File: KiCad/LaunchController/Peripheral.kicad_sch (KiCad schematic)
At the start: 10 parts, among them J15 CONN_AUDIO, J16 CONN_SPEAKER, J21 RJ45, J22 L, J23 R, U2 24LC256, U7 LTC485CN8#PBF

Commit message: 端子台を選定
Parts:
- J15, J16: footprint Connector_JST:JST_XH_B2B-XH-A_1x02_P2.50mm_Vertical -> TSRP_TerminalBlock_Alphaplus:TB401-1-2-E
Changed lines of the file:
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@@
       (effects (font (size 1.27 1.27)))
     )
-    (property "Footprint" "Connector_JST:JST_XH_B2B-XH-A_1x02_P2.50mm_Vertical" (at 67.31 27.94 0)
-      (effects (font (size 1.27 1.27)) hide)
-    )
-    (property "Datasheet" "https://akizukidenshi.com/catalog/g/gC-12247/" (at 67.31 27.94 0)
+    (property "Footprint" "TSRP_TerminalBlock_Alphaplus:TB401-1-2-E" (at 67.31 27.94 0)
+      (effects (font (size 1.27 1.27)) hide)
+    )
+    (property "Datasheet" "https://akizukidenshi.com/catalog/g/gP-01404/" (at 67.31 27.94 0)
       (effects (font (size 1.27 1.27)) hide)
     )
@@
       (effects (font (size 1.27 1.27)))
     )
-    (property "Footprint" "Connector_JST:JST_XH_B2B-XH-A_1x02_P2.50mm_Vertical" (at 67.31 46.99 0)
-      (effects (font (size 1.27 1.27)) hide)
-    )
-    (property "Datasheet" "https://akizukidenshi.com/catalog/g/gC-12247/" (at 67.31 46.99 0)
-      (effects (font (size 1.27 1.27)) hide)
-    )
+    (property "Footprint" "TSRP_TerminalBlock_Alphaplus:TB401-1-2-E" (at 67.31 46.99 0)
+      (effects (font (size 1.27 1.27)) hide)
+    )
+    (property "Datasheet" "https://akizukidenshi.com/catalog/g/gP-01404/" (at 67.31 46.99 0)
+      (effects (font (size 1.27 1.27)) hide)
+    )

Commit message: 配線終わらん
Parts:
- removed J21: RJ45, Connector_RJ:RJ45_Wuerth_7499010001A_Horizontal, symbol Connector:RJ45
- removed J22: L, Connector_PinHeader_2.54mm:PinHeader_1x08_P2.54mm_Vertical, symbol Connector:Conn_01x08_Socket
- removed J23: R, Connector_PinHeader_2.54mm:PinHeader_1x08_P2.54mm_Vertical, symbol Connector:Conn_01x08_Socket
- removed TP13: TP_A, TestPoint:TestPoint_THTPad_D2.5mm_Drill1.2mm, symbol Connector:TestPoint
- removed TP14: TP_B, TestPoint:TestPoint_THTPad_D2.5mm_Drill1.2mm, symbol Connector:TestPoint
- added J10: RJ45, Connector_RJ:RJ45_Wuerth_7499010001A_Horizontal, symbol Connector:RJ45_Shielded
- added U11: DFPlayer, TSRP_Module:DFPlayer-mini, symbol TSRP_Module:DFPlayer-mini
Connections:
- net +5V: now also U11.1 (VCC)
- net GND: now also J10.1, J10.2, J10.3, J10.6, J10.7, J10.8, J10.SH, U11.10 (GND), U11.7 (GND)
- net UART2_RX: now also U11.3 (TX)
- net UART2_TX: now also U11.2 (RX)
- net at R28.2, U7.6 (A): now also J10.5
- net at R28.1, U7.7 (B): now also J10.4
- net at J15.2 (Pin_2): now also U11.5 (DAC_L)
- net at J16.2 (Pin_2): now also U11.6 (SPK2)
- net at J16.1 (Pin_1): now also U11.8 (SPK1)
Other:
- moved on the sheet: R28, U7

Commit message: リセット
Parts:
- renumbered J10 to J11, U11 to U6
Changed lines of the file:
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@@
         )
         (path "/628d040b-43bf-4733-804f-091644a90124/092bb5f6-479a-4342-8285-14bd550a4a8c"
-          (reference "#PWR046") (unit 1)
+          (reference "#PWR059") (unit 1)
         )
       )
@@
         )
         (path "/628d040b-43bf-4733-804f-091644a90124/092bb5f6-479a-4342-8285-14bd550a4a8c"
+          (reference "#PWR060") (unit 1)
+        )
+      )
+    )
+  )
+  (symbol (lib_id "power:GND") (at 76.2 31.75 0) (unit 1)
+    (in_bom yes) (on_board yes) (dnp no) (fields_autoplaced)
+    (property "Reference" "#PWR050" (at 76.2 38.1 0)
+      (effects (font (size 1.27 1.27)) hide)
+    )
+    (property "Value" "GND" (at 76.2 36.83 0)
+      (effects (font (size 1.27 1.27)))
+    )
+    (property "Footprint" "" (at 76.2 31.75 0)
+      (effects (font (size 1.27 1.27)) hide)
+    )
+    (property "Datasheet" "" (at 76.2 31.75 0)
+      (effects (font (size 1.27 1.27)) hide)
+    )
+    (pin "1")
+    (instances
+      (project "LaunchController"
+        (path "/628d040b-43bf-4733-804f-091644a90124"
+          (reference "#PWR050") (unit 1)
+        )
+        (path "/628d040b-43bf-4733-804f-091644a90124/092bb5f6-479a-4342-8285-14bd550a4a8c"
+          (reference "#PWR057") (unit 1)
+        )
+      )
+    )
+  )
+  (symbol (lib_id "Connector_Generic:Conn_01x02") (at 68.58 46.99 180) (unit 1)
+    (in_bom yes) (on_board yes) (dnp no) (fields_autoplaced)
+    (property "Reference" "J16" (at 68.58 39.37 0)
+      (effects (font (size 1.27 1.27)))
+    )
+    (property "Value" "CONN_SPEAKER" (at 68.58 41.91 0)
+      (effects (font (size 1.27 1.27)))
+    )
+    (property "Footprint" "TSRP_TerminalBlock_Alphaplus:TB401-1-2-E" (at 68.58 46.99 0)
+      (effects (font (size 1.27 1.27)) hide)
+    )
+    (property "Datasheet" "https://akizukidenshi.com/catalog/g/gP-01404/" (at 68.58 46.99 0)
+      (effects (font (size 1.27 1.27)) hide)
+    )
+    (pin "1")
+    (pin "2")
+    (instances
+      (project "LaunchController"
+        (path "/628d040b-43bf-4733-804f-091644a90124"
+          (reference "J16") (unit 1)
+        )
+        (path "/628d040b-43bf-4733-804f-091644a90124/092bb5f6-479a-4342-8285-14bd550a4a8c"
+          (reference "J12") (unit 1)
+        )
+      )
+    )
+  )
+  (symbol (lib_id "power:+5V") (at 165.1 19.05 0) (unit 1)
+    (in_bom yes) (on_board yes) (dnp no) (fields_autoplaced)
+    (property "Reference" "#PWR048" (at 165.1 22.86 0)
+      (effects (font (size 1.27 1.27)) hide)
+    )
+    (property "Value" "+5V" (at 165.1 15.24 0)
+      (effects (font (size 1.27 1.27)))
+    )
+    (property "Footprint" "" (at 165.1 19.05 0)
+      (effects (font (size 1.27 1.27)) hide)
+    )
+    (property "Datasheet" "" (at 165.1 19.05 0)
+      (effects (font (size 1.27 1.27)) hide)
+    )
+    (pin "1")
+    (instances
+      (project "LaunchController"
+        (path "/628d040b-43bf-4733-804f-091644a90124"
           (reference "#PWR048") (unit 1)
         )
-      )
-    )
-  )
-  (symbol (lib_id "power:GND") (at 76.2 31.75 0) (unit 1)
-    (in_bom yes) (on_board yes) (dnp no) (fields_autoplaced)
-    (property "Reference" "#PWR050" (at 76.2 38.1 0)
-      (effects (font (size 1.27 1.27)) hide)
-    )
-    (property "Value" "GND" (at 76.2 36.83 0)
-      (effects (font (size 1.27 1.27)))
-    )
-    (property "Footprint" "" (at 76.2 31.75 0)
-      (effects (font (size 1.27 1.27)) hide)
-    )
-    (property "Datasheet" "" (at 76.2 31.75 0)
-      (effects (font (size 1.27 1.27)) hide)
-    )
-    (pin "1")
-    (instances
-      (project "LaunchController"
-        (path "/628d040b-43bf-4733-804f-091644a90124"
-          (reference "#PWR050") (unit 1)
-        )
-        (path "/628d040b-43bf-4733-804f-091644a90124/092bb5f6-479a-4342-8285-14bd550a4a8c"
-          (reference "#PWR039") (unit 1)
-        )
-      )
-    )
-  )
-  (symbol (lib_id "Connector_Generic:Conn_01x02") (at 68.58 46.99 180) (unit 1)
-    (in_bom yes) (on_board yes) (dnp no) (fields_autoplaced)
-    (property "Reference" "J16" (at 68.58 39.37 0)
-      (effects (font (size 1.27 1.27)))
-    )
-    (property "Value" "CONN_SPEAKER" (at 68.58 41.91 0)
-      (effects (font (size 1.27 1.27)))
-    )
-    (property "Footprint" "TSRP_TerminalBlock_Alphaplus:TB401-1-2-E" (at 68.58 46.99 0)
-      (effects (font (size 1.27 1.27)) hide)
-    )
-    (property "Datasheet" "https://akizukidenshi.com/catalog/g/gP-01404/" (at 68.58 46.99 0)
-      (effects (font (size 1.27 1.27)) hide)
-    )
-    (pin "1")
-    (pin "2")
-    (instances
-      (project "LaunchController"
-        (path "/628d040b-43bf-4733-804f-091644a90124"
-          (reference "J16") (unit 1)
-        )
-        (path "/628d040b-43bf-4733-804f-091644a90124/092bb5f6-479a-4342-8285-14bd550a4a8c"
-          (reference "J5") (unit 1)
-        )
-      )
-    )
-  )
-  (symbol (lib_id "power:+5V") (at 165.1 19.05 0) (unit 1)
-    (in_bom yes) (on_board yes) (dnp no) (fields_autoplaced)
-    (property "Reference" "#PWR048" (at 165.1 22.86 0)
-      (effects (font (size 1.27 1.27)) hide)
-    )
-    (property "Value" "+5V" (at 165.1 15.24 0)
-      (effects (font (size 1.27 1.27)))
-    )
-    (property "Footprint" "" (at 165.1 19.05 0)
-      (effects (font (size 1.27 1.27)) hide)
-    )
-    (property "Datasheet" "" (at 165.1 19.05 0)
-      (effects (font (size 1.27 1.27)) hide)
-    )
-    (pin "1")
-    (instances
-      (project "LaunchController"
-        (path "/628d040b-43bf-4733-804f-091644a90124"
-          (reference "#PWR048") (unit 1)
-        )
-        (path "/628d040b-43bf-4733-804f-091644a90124/092bb5f6-479a-4342-8285-14bd550a4a8c"
-          (reference "#PWR043") (unit 1)
+        (path "/628d040b-43bf-4733-804f-091644a90124/092bb5f6-479a-4342-8285-14bd550a4a8c"
+          (reference "#PWR056") (unit 1)
         )
       )
@@
         )
         (path "/628d040b-43bf-4733-804f-091644a90124/092bb5f6-479a-4342-8285-14bd550a4a8c"
-          (reference "R25") (unit 1)
+          (reference "R26") (unit 1)
         )
       )
@@
         )
         (path "/628d040b-43bf-4733-804f-091644a90124/092bb5f6-479a-4342-8285-14bd550a4a8c"
-          (reference "U2") (unit 1)
+          (reference "U7") (unit 1)
         )
       )
@@
         )
         (path "/628d040b-43bf-4733-804f-091644a90124/092bb5f6-479a-4342-8285-14bd550a4a8c"
-          (reference "#PWR014") (unit 1)
+          (reference "#PWR054") (unit 1)
         )
       )
@@
         )
         (path "/628d040b-43bf-4733-804f-091644a90124/092bb5f6-479a-4342-8285-14bd550a4a8c"
-          (reference "#PWR015") (unit 1)
+          (reference "#PWR058") (unit 1)
         )
       )
@@
         )
         (path "/628d040b-43bf-4733-804f-091644a90124/092bb5f6-479a-4342-8285-14bd550a4a8c"
-          (reference "U7") (unit 1)
+          (reference "U8") (unit 1)
         )
       )
@@
         )
         (path "/628d040b-43bf-4733-804f-091644a90124/092bb5f6-479a-4342-8285-14bd550a4a8c"
+          (reference "#PWR055") (unit 1)
+        )
+      )
+    )
+  )
+  (symbol (lib_id "power:GND") (at 165.1 54.61 0) (unit 1)
+    (in_bom yes) (on_board yes) (dnp no) (fields_autoplaced)
+    (property "Reference" "#PWR049" (at 165.1 60.96 0)
+      (effects (font (size 1.27 1.27)) hide)
+    )
+    (property "Value" "GND" (at 165.1 59.69 0)
+      (effects (font (size 1.27 1.27)))
+    )
+    (property "Footprint" "" (at 165.1 54.61 0)
+      (effects (font (size 1.27 1.27)) hide)
+    )
+    (property "Datasheet" "" (at 165.1 54.61 0)
+      (effects (font (size 1.27 1.27)) hide)
+    )
+    (pin "1")
+    (instances
+      (project "LaunchController"
+        (path "/628d040b-43bf-4733-804f-091644a90124"
           (reference "#PWR049") (unit 1)
         )
-      )
-    )
-  )
-  (symbol (lib_id "power:GND") (at 165.1 54.61 0) (unit 1)
-    (in_bom yes) (on_board yes) (dnp no) (fields_autoplaced)
-    (property "Reference" "#PWR049" (at 165.1 60.96 0)
-      (effects (font (size 1.27 1.27)) hide)
-    )
-    (property "Value" "GND" (at 165.1 59.69 0)
-      (effects (font (size 1.27 1.27)))
-    )
-    (property "Footprint" "" (at 165.1 54.61 0)
-      (effects (font (size 1.27 1.27)) hide)
-    )
-    (property "Datasheet" "" (at 165.1 54.61 0)
-      (effects (font (size 1.27 1.27)) hide)
-    )
-    (pin "1")
-    (instances
-      (project "LaunchController"
-        (path "/628d040b-43bf-4733-804f-091644a90124"
-          (reference "#PWR049") (unit 1)
-        )
-        (path "/628d040b-43bf-4733-804f-091644a90124/092bb5f6-479a-4342-8285-14bd550a4a8c"
-          (reference "#PWR045") (unit 1)
+        (path "/628d040b-43bf-4733-804f-091644a90124/092bb5f6-479a-4342-8285-14bd550a4a8c"
+          (reference "#PWR061") (unit 1)
         )
       )
@@
   (symbol (lib_id "TSRP_Module:DFPlayer-mini") (at 102.87 24.13 0) (unit 1)
     (in_bom yes) (on_board yes) (dnp no) (fields_autoplaced)
-    (property "Reference" "U11" (at 114.9859 22.86 0)
+    (property "Reference" "U6" (at 114.9859 22.86 0)
       (effects (font (size 1.27 1.27)) (justify left))
     )
@@
       (project "LaunchController"
         (path "/628d040b-43bf-4733-804f-091644a90124/092bb5f6-479a-4342-8285-14bd550a4a8c"
-          (reference "U11") (unit 1)
+          (reference "U6") (unit 1)
         )
       )
@@
         )
         (path "/628d040b-43bf-4733-804f-091644a90124/092bb5f6-479a-4342-8285-14bd550a4a8c"
-          (reference "J4") (unit 1)
+          (reference "J10") (unit 1)
         )
       )
@@
   (symbol (lib_id "Connector:RJ45_Shielded") (at 209.55 33.02 0) (mirror y) (unit 1)
     (in_bom yes) (on_board yes) (dnp no)
-    (property "Reference" "J10" (at 209.55 16.51 0)
+    (property "Reference" "J11" (at 209.55 16.51 0)
       (effects (font (size 1.27 1.27)))
     )
@@
       (project "LaunchController"
         (path "/628d040b-43bf-4733-804f-091644a90124/092bb5f6-479a-4342-8285-14bd550a4a8c"
-          (reference "J10") (unit 1)
-        )
-      )
+          (reference "J11") (unit 1)
+        )
+      )

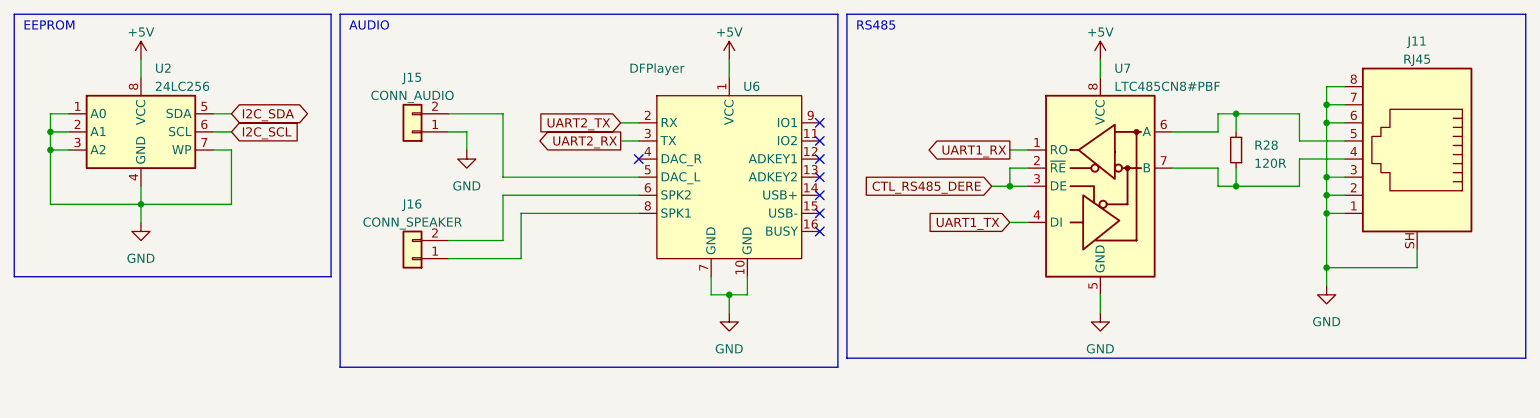
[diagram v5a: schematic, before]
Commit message: 敗北ダイオードを追加
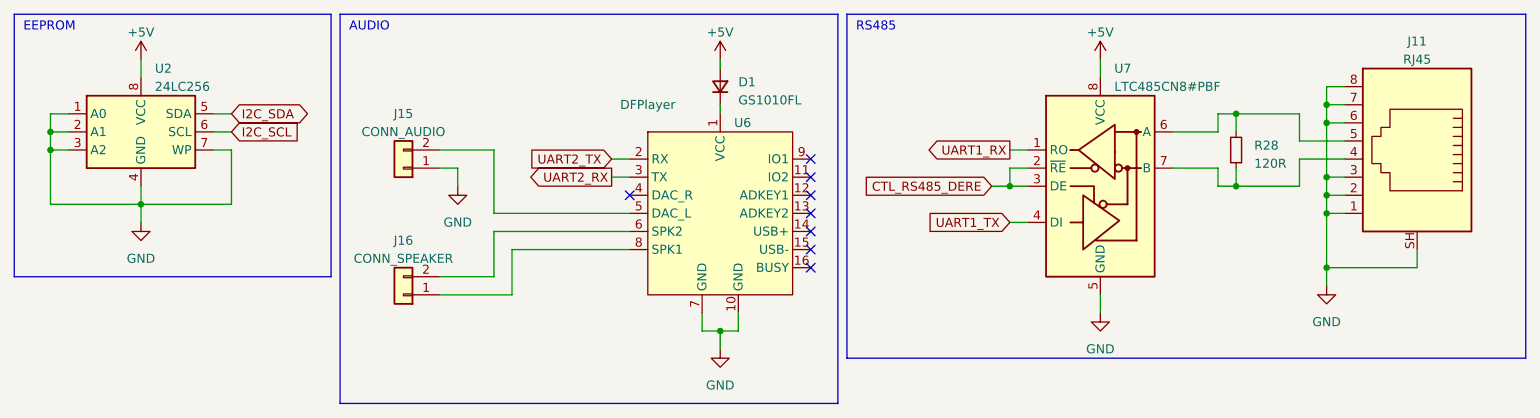
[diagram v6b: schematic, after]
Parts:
- added D1: GS1010FL, Diode_SMD:D_SOD-123F, symbol Device:D_Small
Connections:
- net +5V: now also D1.2 (A); no longer U6.1 (VCC)
- new net: D1.1 (K), U6.1 (VCC)
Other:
- moved on the sheet: J15, J16, U6

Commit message: RJ45をヒロセに変更
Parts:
- J11: footprint Connector_RJ:RJ45_Wuerth_7499010001A_Horizontal -> TSRP_Connector_Hirose:TM11R-5M2-88
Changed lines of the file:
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@@
       (effects (font (size 1.27 1.27)))
     )
-    (property "Footprint" "Connector_RJ:RJ45_Wuerth_7499010001A_Horizontal" (at 209.55 32.385 90)
+    (property "Footprint" "TSRP_Connector_Hirose:TM11R-5M2-88" (at 209.55 32.385 90)
       (effects (font (size 1.27 1.27)) hide)
     )
